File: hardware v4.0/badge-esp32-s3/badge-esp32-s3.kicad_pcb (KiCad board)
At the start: 2 copper layers, 131.5 x 83.5 mm, 214 parts, among them CN1 B4B-PH-SM4-TB (LF)(SN), J1 Connector, USB-TYPE-C-16P, J11 Conn_02x03_Odd_Even, J12 Conn_01x02_Socket, J13 Conn_01x04_Socket, J14 Conn_01x02_Socket, J15 Conn_01x02_Socket, J2 Connector, USB-TYPE-C-16P, J3 Conn_02x06_Odd_Even, J4 Conn_02x15_Odd_Even, J5 Conn_01x02_Socket, J6 Conn_01x04_Socket, J7 Conn_01x08_Socket, J8 Conn_01x08_Socket, J9 Conn_02x06_Odd_Even, P1 PH-2A_C2319, P2 FPC 0.5MM 12P Pull type H2.0m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, P3 WJ124-3.81-2P, Q1 SS8050 200-350, Q10 DMN3150L-7, Q11 DMN3150L-7, Q2 SS8050 200-350, Q3 AP1606, Q5 DTC114E, Q6 SI2301CDS-T1-GE3, SW1 TS-1088-AR02016, SW10 SK22D02G5, SW2 TS-1088-AR02016, SW4 TS665CJ, SW5 TS665CJ, SW6 TS665CJ, SW7 TS665CJ, SW8 TS665CJ, SW9 TS665CJ, U1 ESP32-S3-MINI-1-N4R2, U11 SY6288F1ABC, U12 SY6288F1ABC, U18 MMA8452QR1_C11360, U2 TPS630701RNMR, U3 CP2102N-A02-GQFN28R, U4 TP4056, U5 TPS2121RUXR, U6 ZX-SH1.0-4PWT, U7 HS20HS072RX-fpc, U8 TUSB321AIRWBR, U9 AP63203WU-7

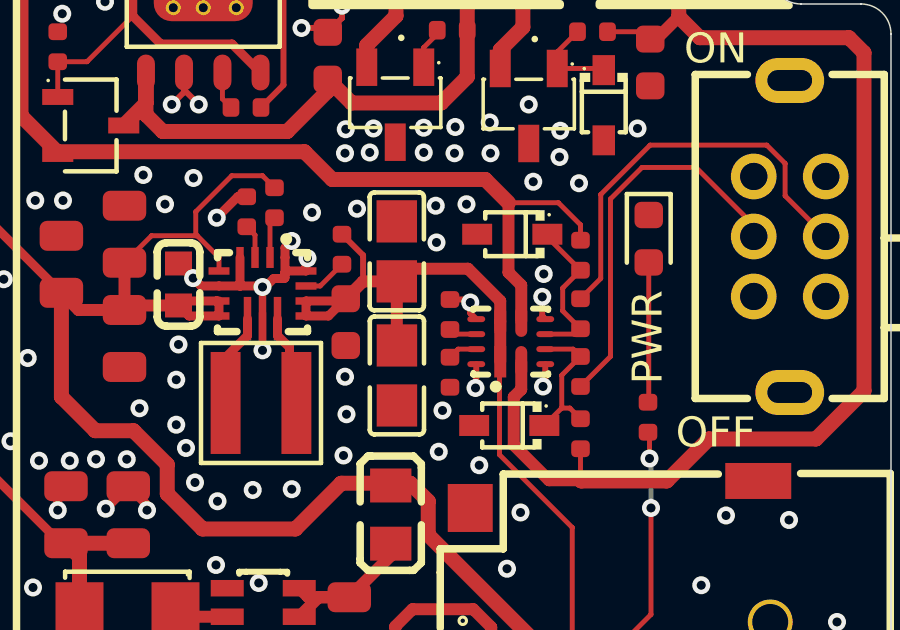
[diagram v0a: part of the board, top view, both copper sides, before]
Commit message: changed PWR switch and current limit
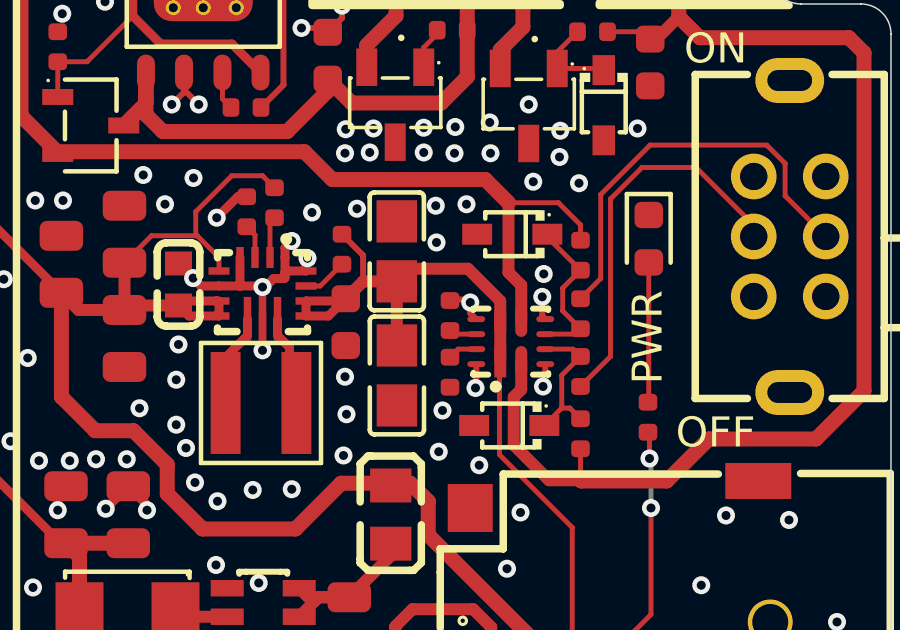
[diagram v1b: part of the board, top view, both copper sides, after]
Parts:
- removed R58: 47kΩ, PCM_JLCPCB:R_0402
- added R63: 39kΩ, PCM_JLCPCB:R_0402, F.Cu at (196.8, 104.8)
